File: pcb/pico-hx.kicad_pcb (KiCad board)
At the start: 4 copper layers, 80.7 x 65.8 mm, 75 parts, among them J1 PMOD_A, J2 PMOD_B, J3 Micro_SD, J4 PMOD_C, J5 PMOD_D, J6 UART, J7 RP_SWD, J8 5V_AB, J9 5V_CD, SW1 RUN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

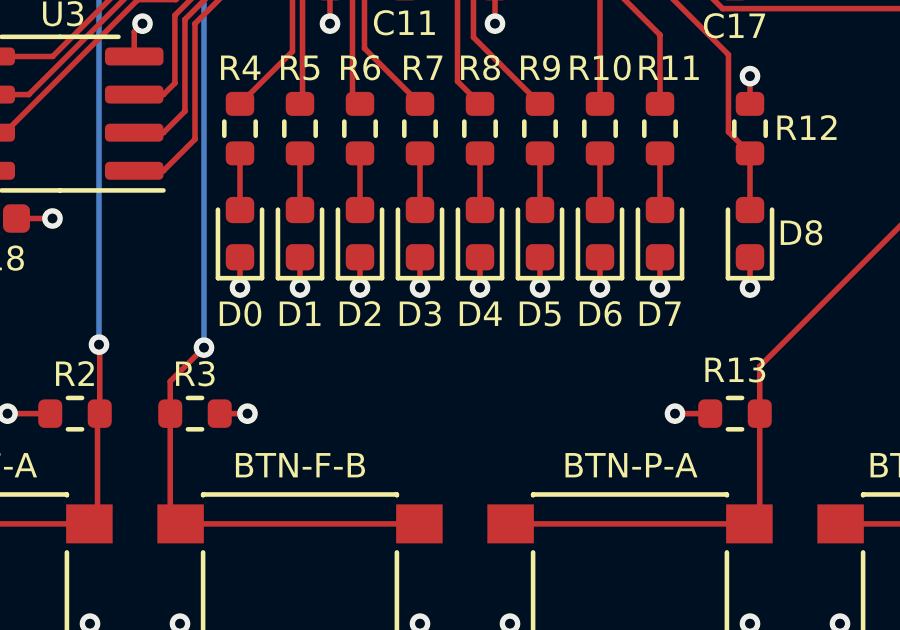
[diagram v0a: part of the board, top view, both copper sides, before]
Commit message: pcb: reverse LED order to be more intuitive
Previously the LSB was on the right and the MSB was on left.
Outputting an 8bit value for example would be confusing if interpreting it as a binary representation.
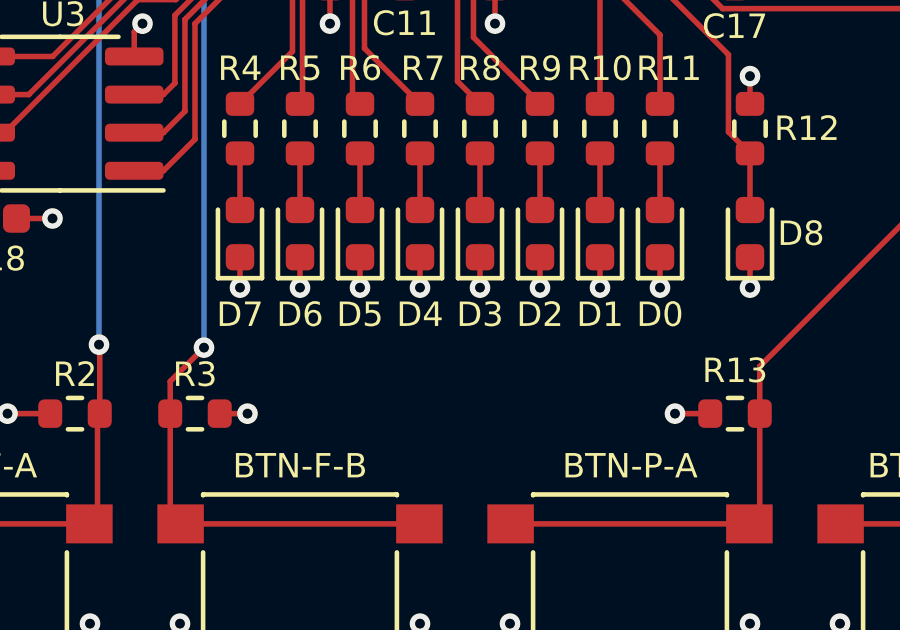
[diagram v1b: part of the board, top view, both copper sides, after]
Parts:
- moved D0 14.0 mm to (104.5, 99.5)
- moved D7 14.0 mm to (90.5, 99.5)
- moved D1 10.0 mm to (102.5, 99.5)
- moved D6 10.0 mm to (92.5, 99.5)
- moved D2 6.00 mm to (100.5, 99.5)
- moved D5 6.00 mm to (94.5, 99.5)
- moved D3 2.00 mm to (98.5, 99.5)
- moved D4 2.00 mm to (96.5, 99.5)
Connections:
- R10 pad 1: /LED_6 -> /LED_1
- R10 pad 2: Net-(D6-Pad2) -> Net-(D1-Pad2)
- R11 pad 1: /LED_7 -> /LED_0
- R11 pad 2: Net-(D7-Pad2) -> Net-(D0-Pad2)
- R4 pad 1: /LED_0 -> /LED_7
- R4 pad 2: Net-(D0-Pad2) -> Net-(D7-Pad2)
- R5 pad 1: /LED_1 -> /LED_6
- R5 pad 2: Net-(D1-Pad2) -> Net-(D6-Pad2)
- R6 pad 1: /LED_2 -> /LED_5
- R6 pad 2: Net-(D2-Pad2) -> Net-(D5-Pad2)
- R7 pad 1: /LED_3 -> /LED_4
- R7 pad 2: Net-(D3-Pad2) -> Net-(D4-Pad2)
- R8 pad 1: /LED_4 -> /LED_3
- R8 pad 2: Net-(D4-Pad2) -> Net-(D3-Pad2)
- R9 pad 1: /LED_5 -> /LED_2
- R9 pad 2: Net-(D5-Pad2) -> Net-(D2-Pad2)
- U2 pad 44: /LED_0 -> /LED_7
- U2 pad 45: /LED_1 -> /LED_6
- U2 pad 47: /LED_2 -> /LED_5
- U2 pad 48: /LED_3 -> /LED_4
- U2 pad 52: /LED_4 -> /LED_3
- U2 pad 56: /LED_5 -> /LED_2
- U2 pad 58: /LED_6 -> /LED_1
- U2 pad 60: /LED_7 -> /LED_0
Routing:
- net /LED_5: track 8.48 -> 7.56 mm
- net /LED_2: track 7.56 -> 8.48 mm
- net /LED_6: track 8.59 -> 7.68 mm
- net /LED_1: track 7.68 -> 8.59 mm
- net /LED_7: track 9.01 -> 8.30 mm
- net /LED_0: track 8.30 -> 9.01 mm

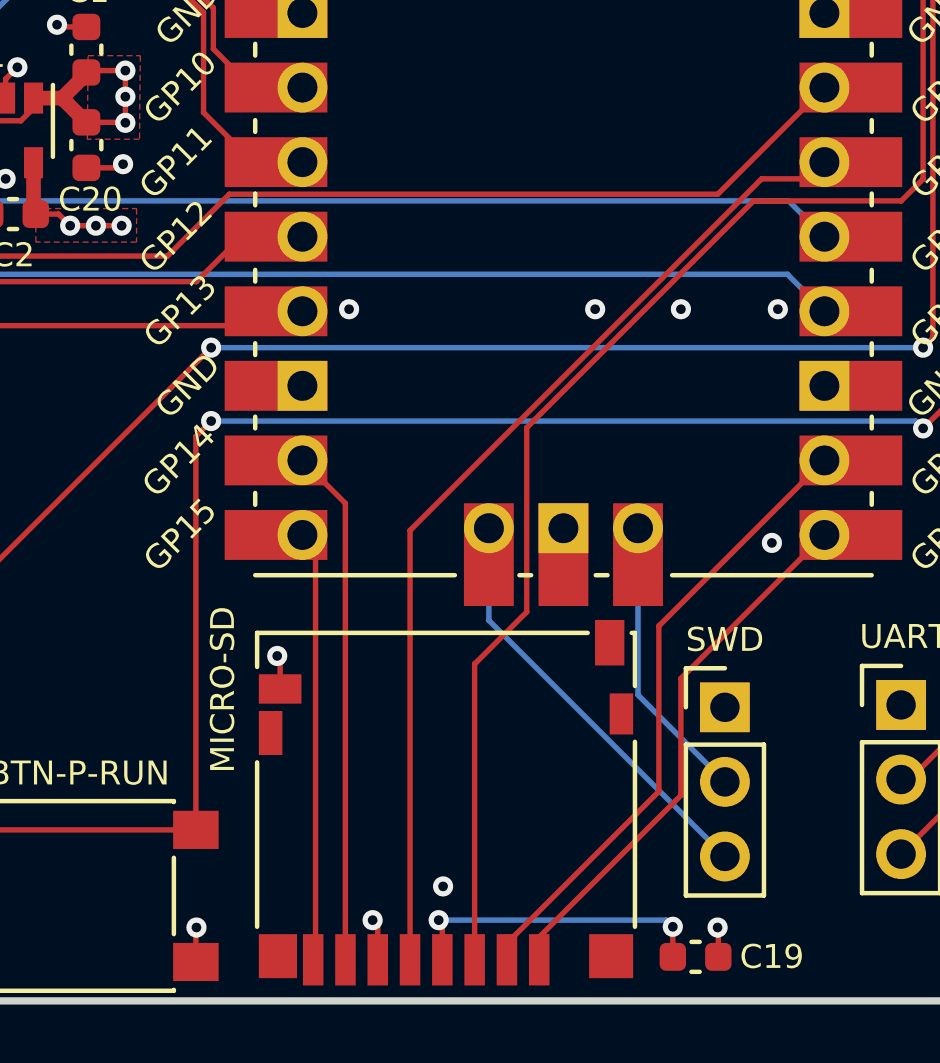
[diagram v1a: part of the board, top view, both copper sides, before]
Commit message: pcb: add copper-keepout for SD card connector
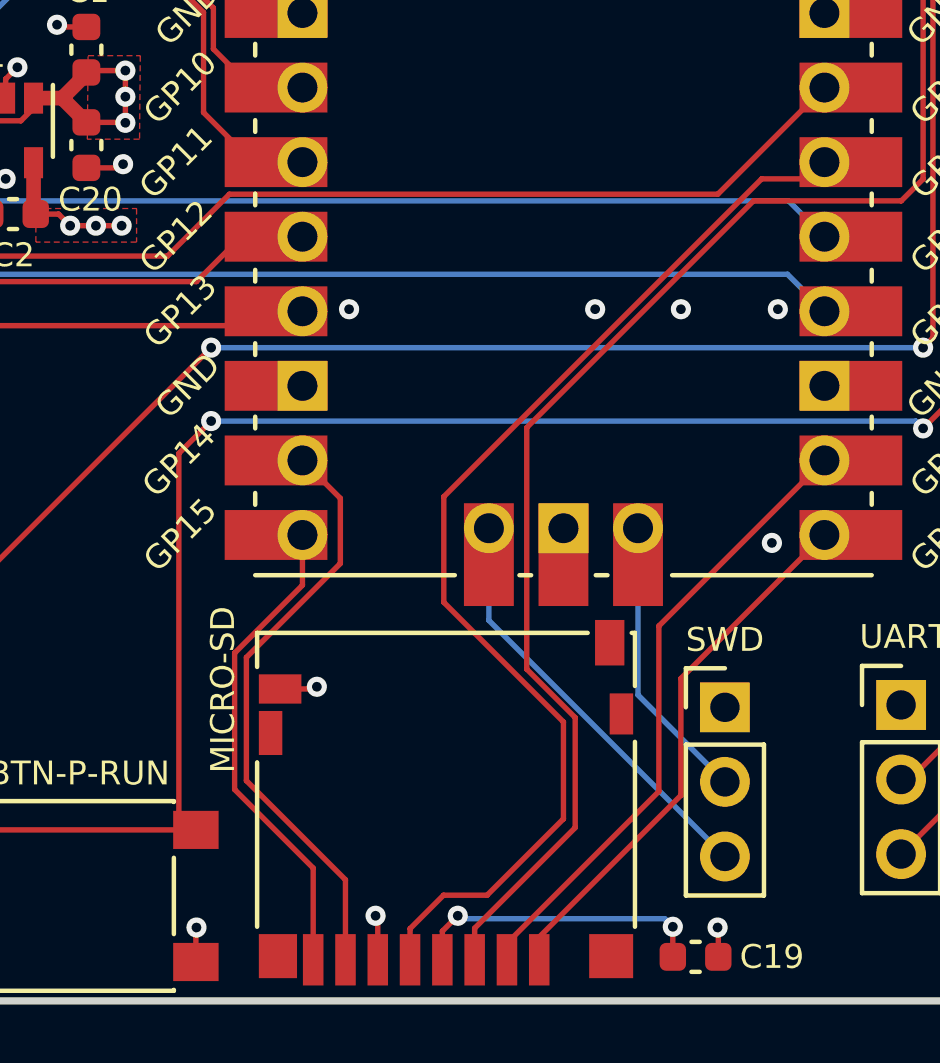
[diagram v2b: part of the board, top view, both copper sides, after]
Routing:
- net /SD_CLK: track 33.9 -> 38.2 mm
- net /SD_DAT0: track 17.6 -> 20.3 mm
- net /SD_DAT1: track 14.7 -> 16.5 mm
- net /SD_CMD: track 46.3 -> 47.6 mm
- net GND: track 57.0 -> 57.2 mm, vias 70 -> 69
